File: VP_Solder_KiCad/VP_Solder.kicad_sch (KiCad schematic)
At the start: 141 parts, among them J1 Conn_01x04, SW1 SW_Push, SW2 SW_Push, U1 STM32F072CBTx, U2 XC6206PxxxMR, U3 USBLC6-2SC6

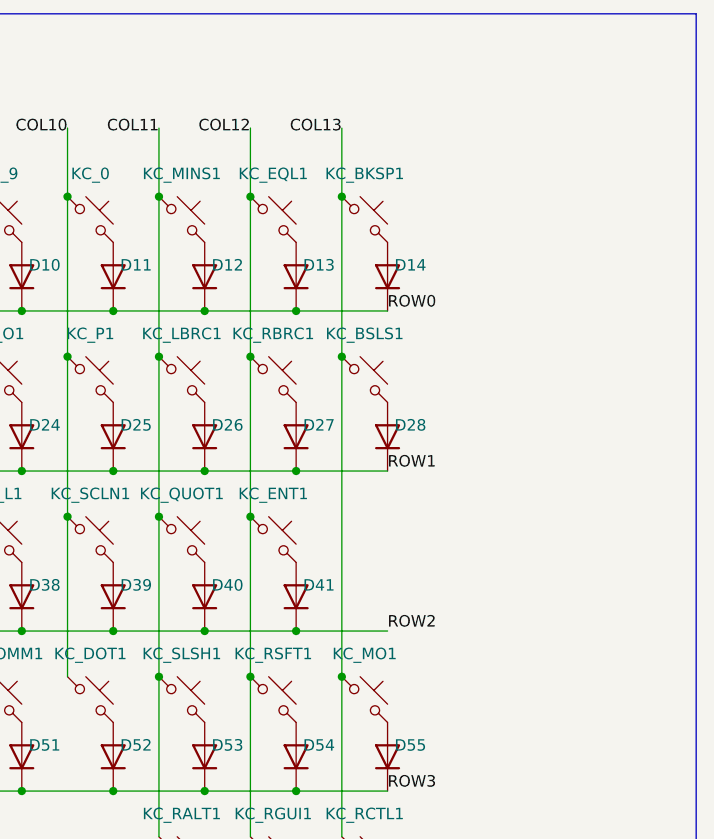
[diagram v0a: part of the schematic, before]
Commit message: Added split backspace
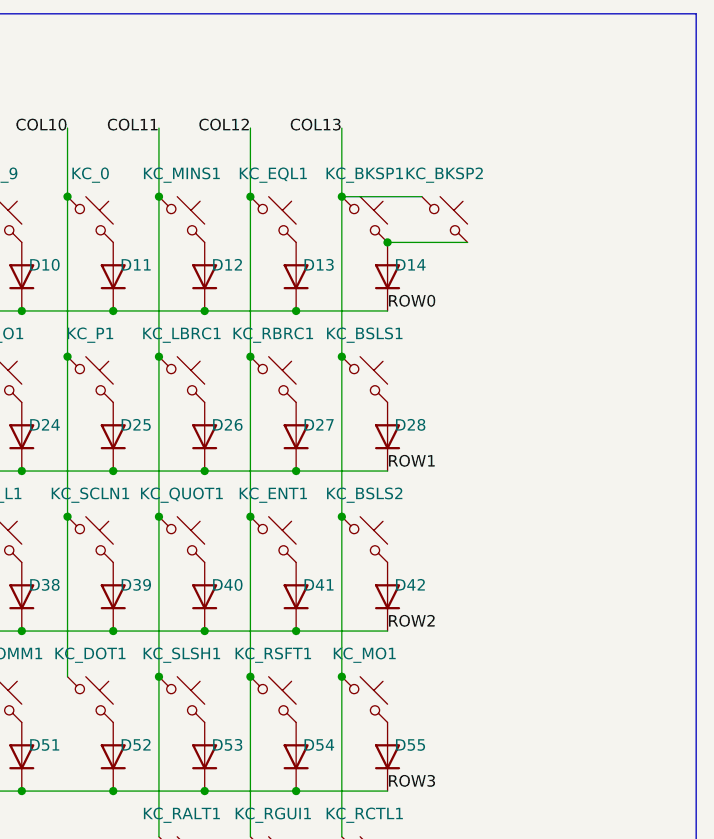
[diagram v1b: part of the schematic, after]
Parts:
- added D42: 1N4148, Diode_SMD:D_SOD-123, symbol Diode:1N4148
- added KC_BKSP2, KC_BSLS2: MX_SW_solder, marbastlib-mx:SW_MX_1u, symbol marbastlib-mx:MX_SW_solder
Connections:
- net COL13: now also KC_BKSP2.1, KC_BSLS2.1
- net ROW2: now also D42.1 (K)
- net at D14.2 (A), KC_BKSP1.2: now also KC_BKSP2.2
- new net: D42.2 (A), KC_BSLS2.2

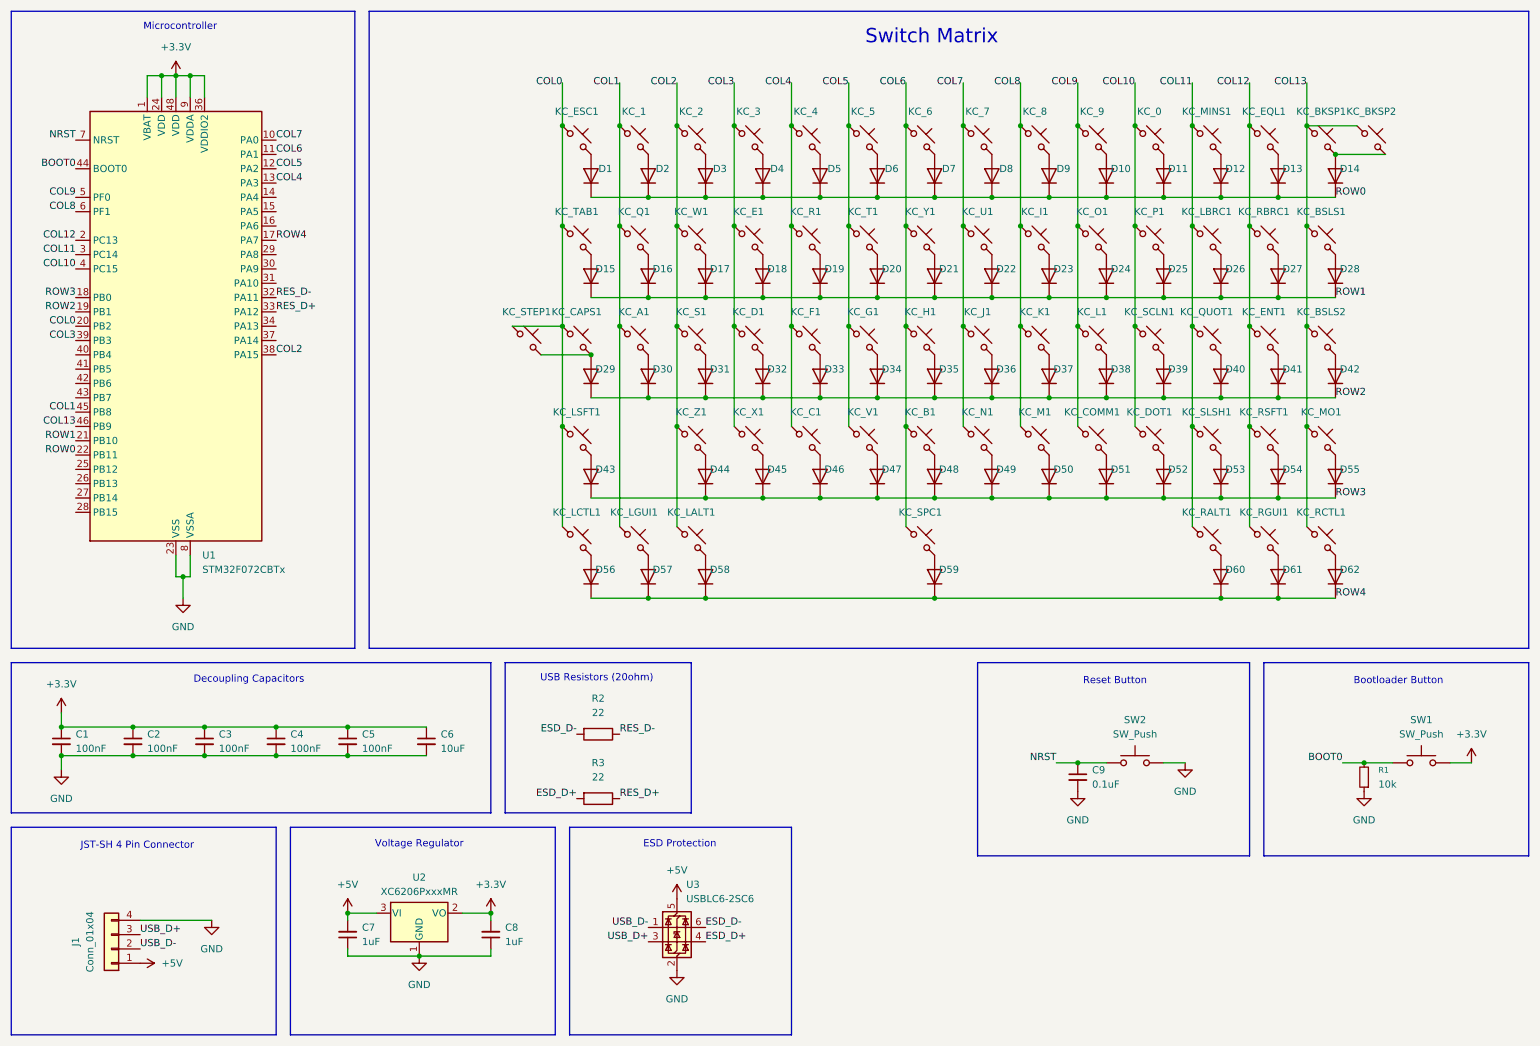
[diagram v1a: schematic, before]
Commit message: Added testpoints
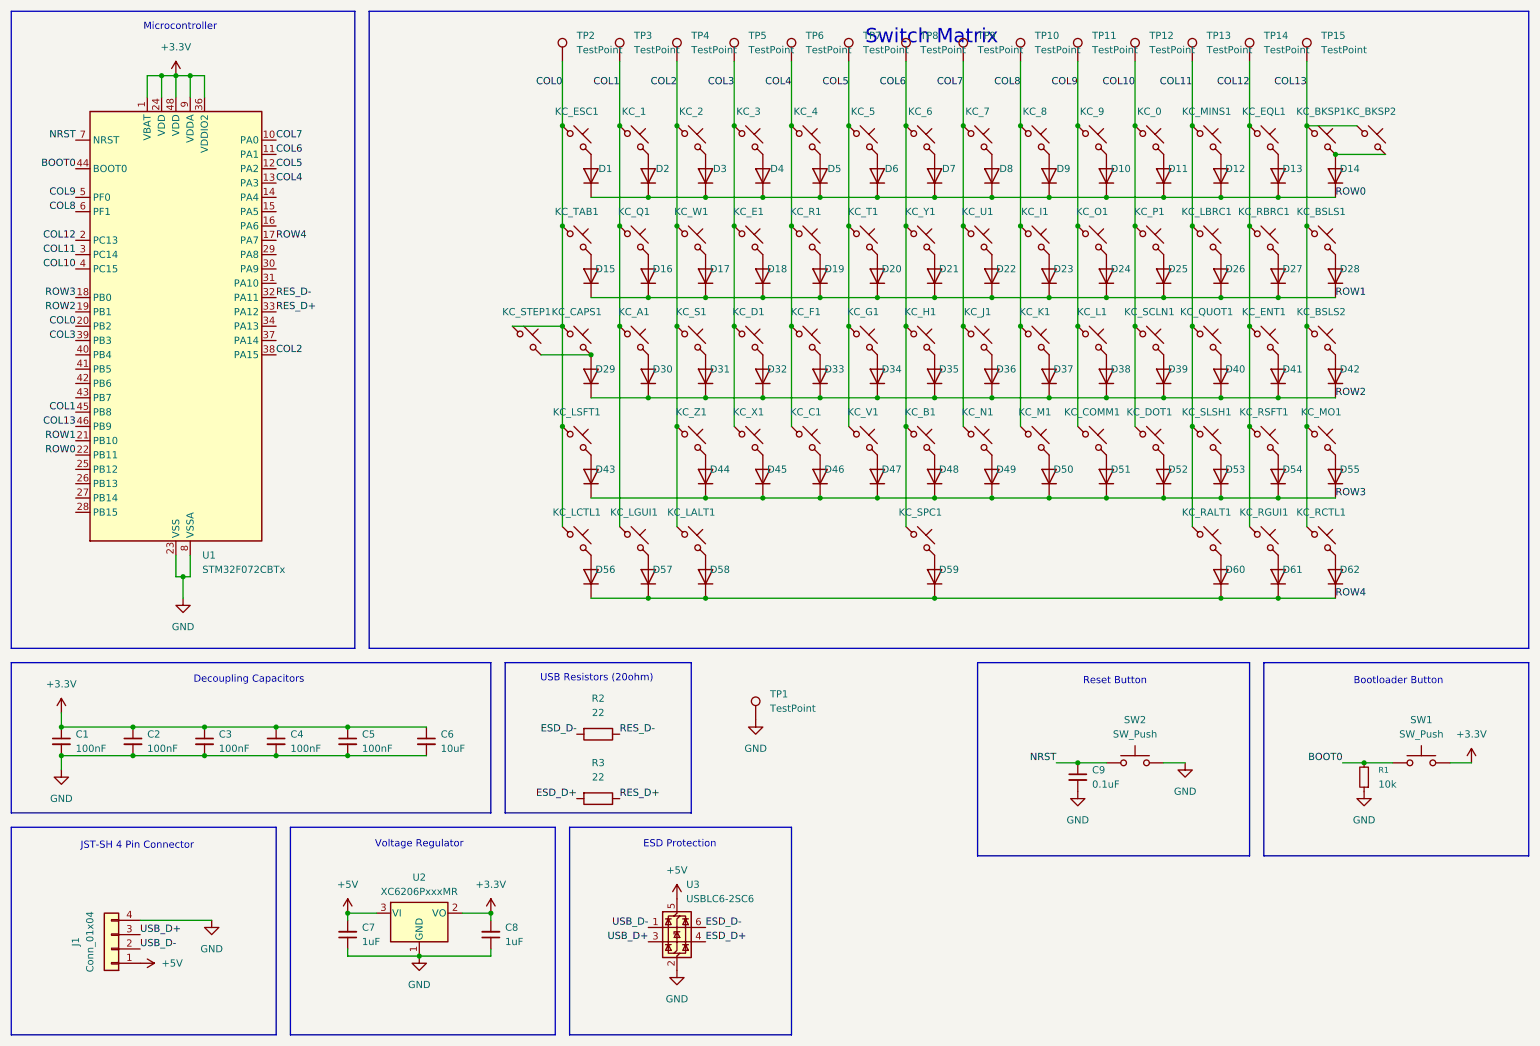
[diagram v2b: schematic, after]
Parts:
- added TP1: TestPoint, TestPoint:TestPoint_Bridge_Pitch2.0mm_Drill0.7mm, symbol Connector:TestPoint
- added TP10, TP11, TP12, TP13, TP14, TP15, TP2, TP3, TP4, TP5, TP6, TP7, TP8, TP9: TestPoint, TestPoint:TestPoint_Pad_1.5x1.5mm, symbol Connector:TestPoint
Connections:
- net COL0: now also TP2.1
- net COL1: now also TP3.1
- net COL10: now also TP12.1
- net COL11: now also TP13.1
- net COL12: now also TP14.1
- net COL13: now also TP15.1
- net COL2: now also TP4.1
- net COL3: now also TP5.1
- net COL4: now also TP6.1
- net COL5: now also TP7.1
- net COL6: now also TP8.1
- net COL7: now also TP9.1
- net COL8: now also TP10.1
- net COL9: now also TP11.1
- net GND: now also TP1.1
